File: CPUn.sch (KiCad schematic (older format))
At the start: 11 parts, among them J4 JTAG

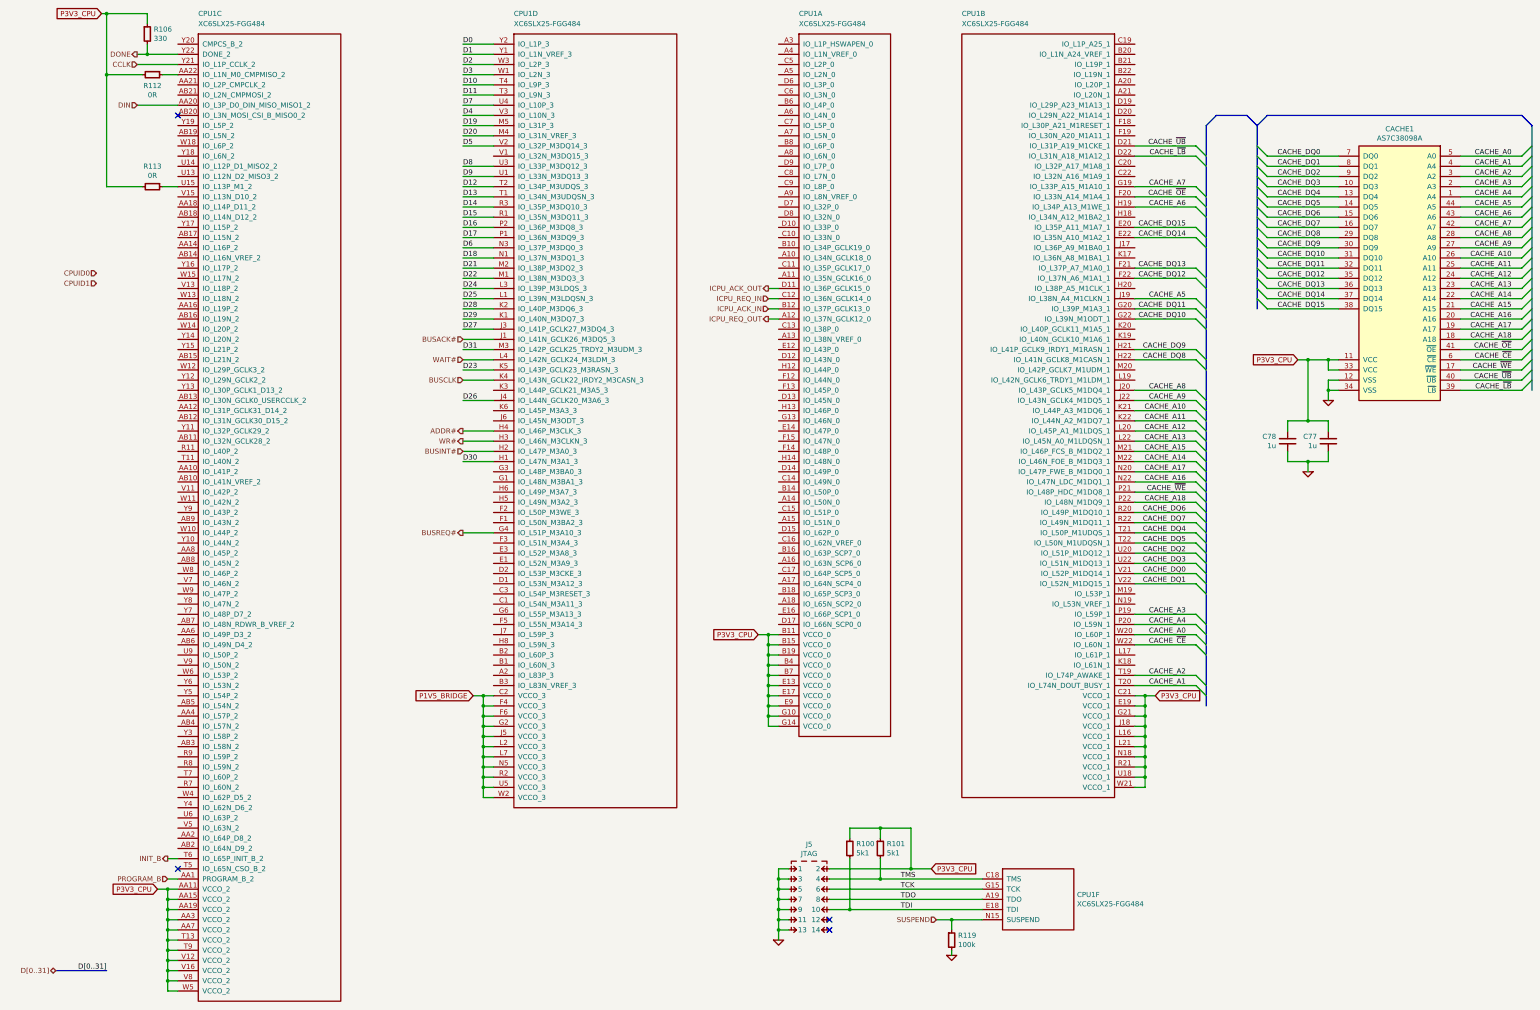
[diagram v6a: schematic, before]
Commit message: Rename active-low signals for consistency
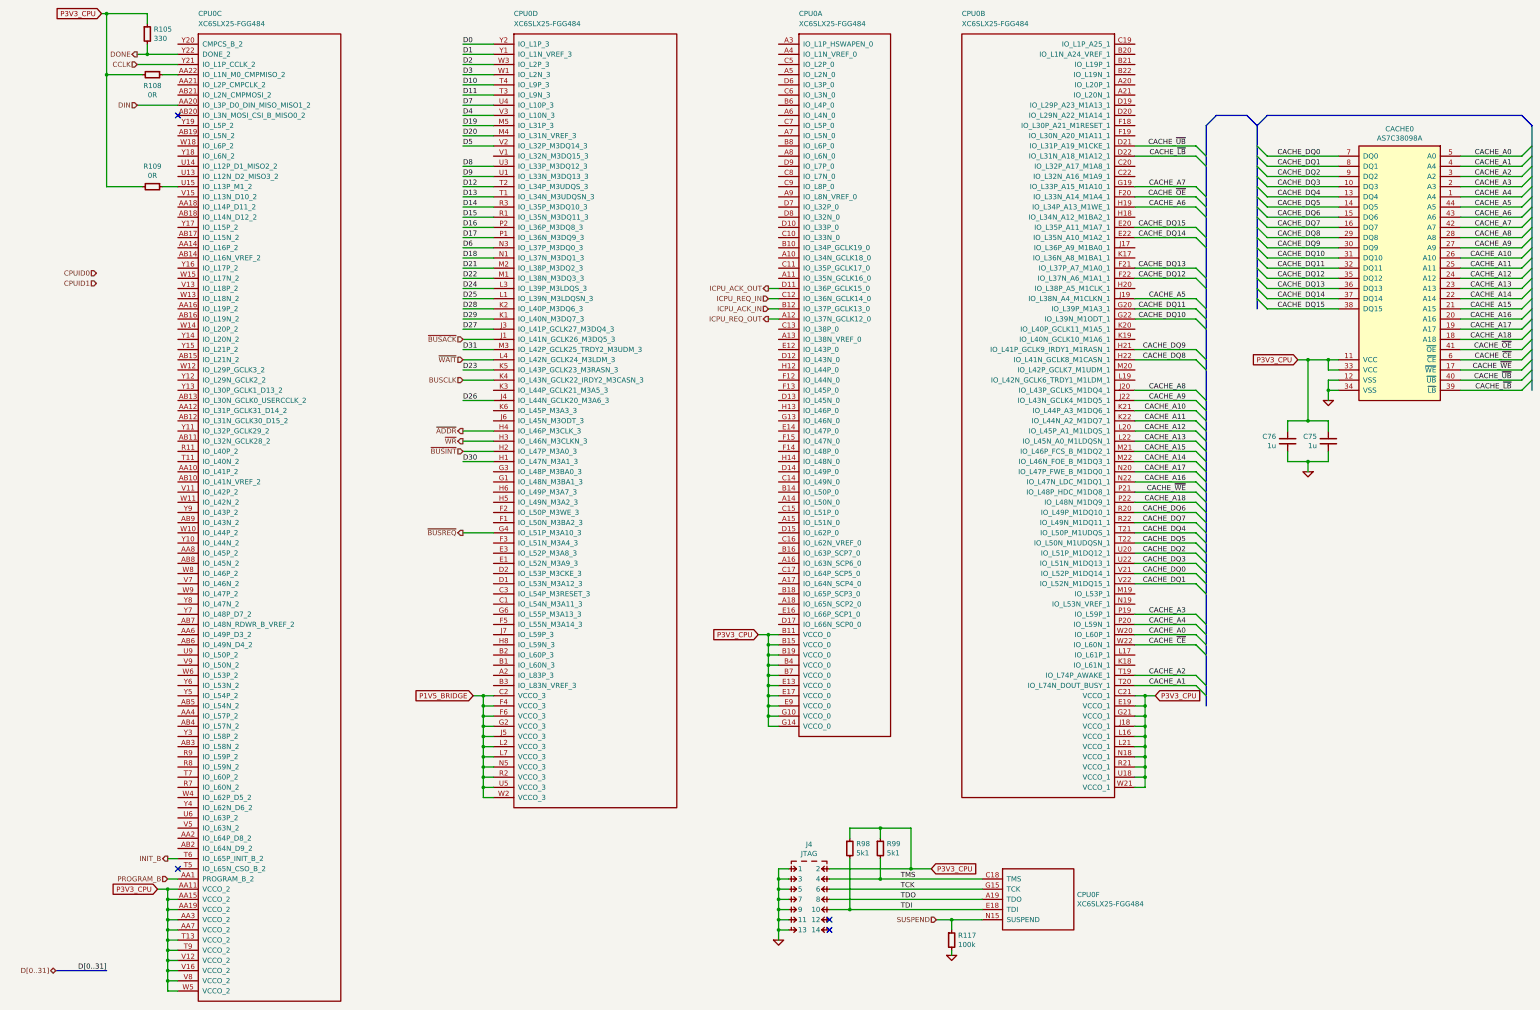
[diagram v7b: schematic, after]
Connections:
- net ADDR# renamed ~ADDR
- net BUSACK# renamed ~BUSACK
- net BUSINT# renamed ~BUSINT
- net BUSREQ# renamed ~BUSREQ
- net WAIT# renamed ~WAIT
- net WR# renamed ~WR
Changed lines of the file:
@@
 $Descr B 17000 11000
 encoding utf-8
-Sheet 9 10
+Sheet 4 10
 Title "CPU"
 Date "2016-08-05"
@@
 AR Path="/5765A5BA/577B458D" Ref="CPU0"  Part="3"
 AR Path="/5765B2E6/577B458D" Ref="CPU1"  Part="3"
-F 0 "CPU1" H 2500 1300 50  0000 L CNN
+F 0 "CPU0" H 2500 1300 50  0000 L CNN
 F 1 "XC6SLX25-FGG484" H 2500 1200 50  0000 L CNN
 F 2 "manuf:XILINX-FGG484" H 2400 1150 50  0001 C CNN
@@
 D[0..31]
 Text HLabel 5100 4100 0    50   Input ~ 0
-WAIT#
+~WAIT
 Text HLabel 5100 4800 0    50   Output ~ 0
-ADDR#
+~ADDR
 Text HLabel 5100 4900 0    50   Output ~ 0
-WR#
+~WR
 Text HLabel 5100 5800 0    50   Output ~ 0
-BUSREQ#
+~BUSREQ
 Text HLabel 5100 3900 0    50   Input ~ 0
-BUSACK#
+~BUSACK
 Text HLabel 5100 5000 0    50   Input ~ 0
-BUSINT#
+~BUSINT
 Text GLabel 2100 9300 0    50   Input ~ 0
 P3V3_CPU
@@
 AR Path="/5765A5BA/5783D342" Ref="CACHE0"  Part="1"
 AR Path="/5765B2E6/5783D342" Ref="CACHE1"  Part="1"
-F 0 "CACHE1" H 14300 2367 50  0000 C CNN
+F 0 "CACHE0" H 14300 2367 50  0000 C CNN
 F 1 "AS7C38098A" H 14300 2276 50  0000 C CNN
 F 2 "IPC7351-Nominal:SOP80P1176X120-44" H 14300 -400 50  0001 C CNN
@@
 AR Path="/5765A5BA/5793B4AE" Ref="#PWR122"  Part="1"
 AR Path="/5765B2E6/5793B4AE" Ref="#PWR184"  Part="1"
-F 0 "#PWR184" H 13600 4500 30  0001 C CNN
+F 0 "#PWR122" H 13600 4500 30  0001 C CNN
 F 1 "GND" H 13600 4430 30  0001 C CNN
 F 2 "" H 13600 4500 60  0000 C CNN
@@
 AR Path="/5765A5BA/5793BAAD" Ref="C75"  Part="1"
 AR Path="/5765B2E6/5793BAAD" Ref="C77"  Part="1"
-F 0 "C77" H 13712 4946 50  0000 L CNN
+F 0 "C75" H 13712 4946 50  0000 L CNN
 F 1 "1u" H 13712 4855 50  0000 L CNN
 F 2 "IPC7351-Nominal:CAPC1005X55" H 13600 4900 50  0001 C CNN
@@
 AR Path="/5765A5BA/5793BB4A" Ref="C76"  Part="1"
 AR Path="/5765B2E6/5793BB4A" Ref="C78"  Part="1"
-F 0 "C78" H 13313 4946 50  0000 L CNN
+F 0 "C76" H 13313 4946 50  0000 L CNN
 F 1 "1u" H 13313 4855 50  0000 L CNN
 F 2 "IPC7351-Nominal:CAPC1005X55" H 13200 4900 50  0001 C CNN
@@
 AR Path="/5765A5BA/5793BC86" Ref="#PWR121"  Part="1"
 AR Path="/5765B2E6/5793BC86" Ref="#PWR183"  Part="1"
-F 0 "#PWR183" H 13400 5200 30  0001 C CNN
+F 0 "#PWR121" H 13400 5200 30  0001 C CNN
 F 1 "GND" H 13400 5130 30  0001 C CNN
 F 2 "" H 13400 5200 60  0000 C CNN
@@
 AR Path="/5765A5BA/57942A58" Ref="CPU0"  Part="4"
 AR Path="/5765B2E6/57942A58" Ref="CPU1"  Part="4"
-F 0 "CPU1" H 5600 1300 50  0000 L CNN
+F 0 "CPU0" H 5600 1300 50  0000 L CNN
 F 1 "XC6SLX25-FGG484" H 5600 1200 50  0000 L CNN
 F 2 "manuf:XILINX-FGG484" H 5500 1150 50  0001 C CNN
@@
 AR Path="/5765A5BA/5795C53B" Ref="CPU0"  Part="1"
 AR Path="/5765B2E6/5795C53B" Ref="CPU1"  Part="1"
-F 0 "CPU1" H 8400 1300 50  0000 L CNN
+F 0 "CPU0" H 8400 1300 50  0000 L CNN
 F 1 "XC6SLX25-FGG484" H 8400 1200 50  0000 L CNN
 F 2 "manuf:XILINX-FGG484" H 8300 1150 50  0001 C CNN
@@
 AR Path="/5765A5BA/5795C751" Ref="CPU0"  Part="2"
 AR Path="/5765B2E6/5795C751" Ref="CPU1"  Part="2"
-F 0 "CPU1" H 13400 1300 50  0000 R CNN
+F 0 "CPU0" H 13400 1300 50  0000 R CNN
 F 1 "XC6SLX25-FGG484" H 13400 1200 50  0000 R CNN
 F 2 "manuf:XILINX-FGG484" H 11800 1150 50  0001 C CNN
@@
 AR Path="/5765A5BA/57A58F79" Ref="R105"  Part="1"
 AR Path="/5765B2E6/57A58F79" Ref="R106"  Part="1"
-F 0 "R106" H 2063 946 50  0000 L CNN
+F 0 "R105" H 2063 946 50  0000 L CNN
 F 1 "330" H 2063 855 50  0000 L CNN
 F 2 "IPC7351-Nominal:RESC1005X40" H 2000 900 50  0001 C CNN
@@
 AR Path="/5765A5BA/57A5D20B" Ref="R108"  Part="1"
 AR Path="/5765B2E6/57A5D20B" Ref="R112"  Part="1"
-F 0 "R112" V 2158 1300 50  0000 C CNN
+F 0 "R108" V 2158 1300 50  0000 C CNN
 F 1 "0R" V 2249 1300 50  0000 C CNN
 F 2 "IPC7351-Nominal:RESC1005X40" H 2050 1300 50  0001 C CNN
@@
 AR Path="/5765A5BA/57A5D251" Ref="R109"  Part="1"
 AR Path="/5765B2E6/57A5D251" Ref="R113"  Part="1"
-F 0 "R113" V 1850 2400 50  0000 C CNN
+F 0 "R109" V 1850 2400 50  0000 C CNN
 F 1 "0R" V 1941 2400 50  0000 C CNN
 F 2 "IPC7351-Nominal:RESC1005X40" H 2050 2400 50  0001 C CNN
@@
 AR Path="/5765A5BA/57A7F2F7" Ref="J4"  Part="1"
 AR Path="/5765B2E6/57A7F2F7" Ref="J5"  Part="1"
-F 0 "J5" H 8500 9340 50  0000 C CNN
+F 0 "J4" H 8500 9340 50  0000 C CNN
 F 1 "JTAG" H 8500 9249 50  0000 C CNN
 F 2 "conn-fci:98424-G52-14ALF" H 8475 9100 50  0001 C CNN
@@
 AR Path="/5765B2E6/57A7F302" Ref="#PWR181"  Part="1"
 AR Path="/5765A5BA/57A7F302" Ref="#PWR119"  Part="1"
-F 0 "#PWR181" H 8200 9800 30  0001 C CNN
+F 0 "#PWR119" H 8200 9800 30  0001 C CNN
 F 1 "GND" H 8200 9730 30  0001 C CNN
 F 2 "" H 8200 9800 60  0000 C CNN
@@
 AR Path="/5765A5BA/57A7F317" Ref="R98"  Part="1"
 AR Path="/5765B2E6/57A7F317" Ref="R100"  Part="1"
-F 0 "R100" H 8963 8946 50  0000 L CNN
+F 0 "R98" H 8963 8946 50  0000 L CNN
 F 1 "5k1" H 8963 8855 50  0000 L CNN
 F 2 "IPC7351-Nominal:RESC1005X40" H 8900 8900 50  0001 C CNN
@@
 AR Path="/5765A5BA/57A7F321" Ref="R99"  Part="1"
 AR Path="/5765B2E6/57A7F321" Ref="R101"  Part="1"
-F 0 "R101" H 9263 8946 50  0000 L CNN
+F 0 "R99" H 9263 8946 50  0000 L CNN
 F 1 "5k1" H 9263 8855 50  0000 L CNN
 F 2 "IPC7351-Nominal:RESC1005X40" H 9200 8900 50  0001 C CNN
@@
 AR Path="/5765A5BA/57A7F34A" Ref="CPU0"  Part="6"
 AR Path="/5765B2E6/57A7F34A" Ref="CPU1"  Part="6"
-F 0 "CPU1" H 11131 9046 50  0000 L CNN
+F 0 "CPU0" H 11131 9046 50  0000 L CNN
 F 1 "XC6SLX25-FGG484" H 11131 8955 50  0000 L CNN
 F 2 "manuf:XILINX-FGG484" H 10300 9350 50  0001 C CNN
@@
 AR Path="/5765A5BA/57A6CB4C" Ref="R117"  Part="1"
 AR Path="/5765B2E6/57A6CB4C" Ref="R119"  Part="1"
-F 0 "R119" H 9963 9846 50  0000 L CNN
+F 0 "R117" H 9963 9846 50  0000 L CNN
 F 1 "100k" H 9963 9755 50  0000 L CNN
 F 2 "IPC7351-Nominal:RESC1005X40" H 9900 9800 50  0001 C CNN
@@
 AR Path="/5765A5BA/57A6CCC5" Ref="#PWR120"  Part="1"
 AR Path="/5765B2E6/57A6CCC5" Ref="#PWR182"  Part="1"
-F 0 "#PWR182" H 9900 9950 30  0001 C CNN
+F 0 "#PWR120" H 9900 9950 30  0001 C CNN
 F 1 "GND" H 9900 9880 30  0001 C CNN
 F 2 "" H 9900 9950 60  0000 C CNN

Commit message: Route unused PCI JTAG lines
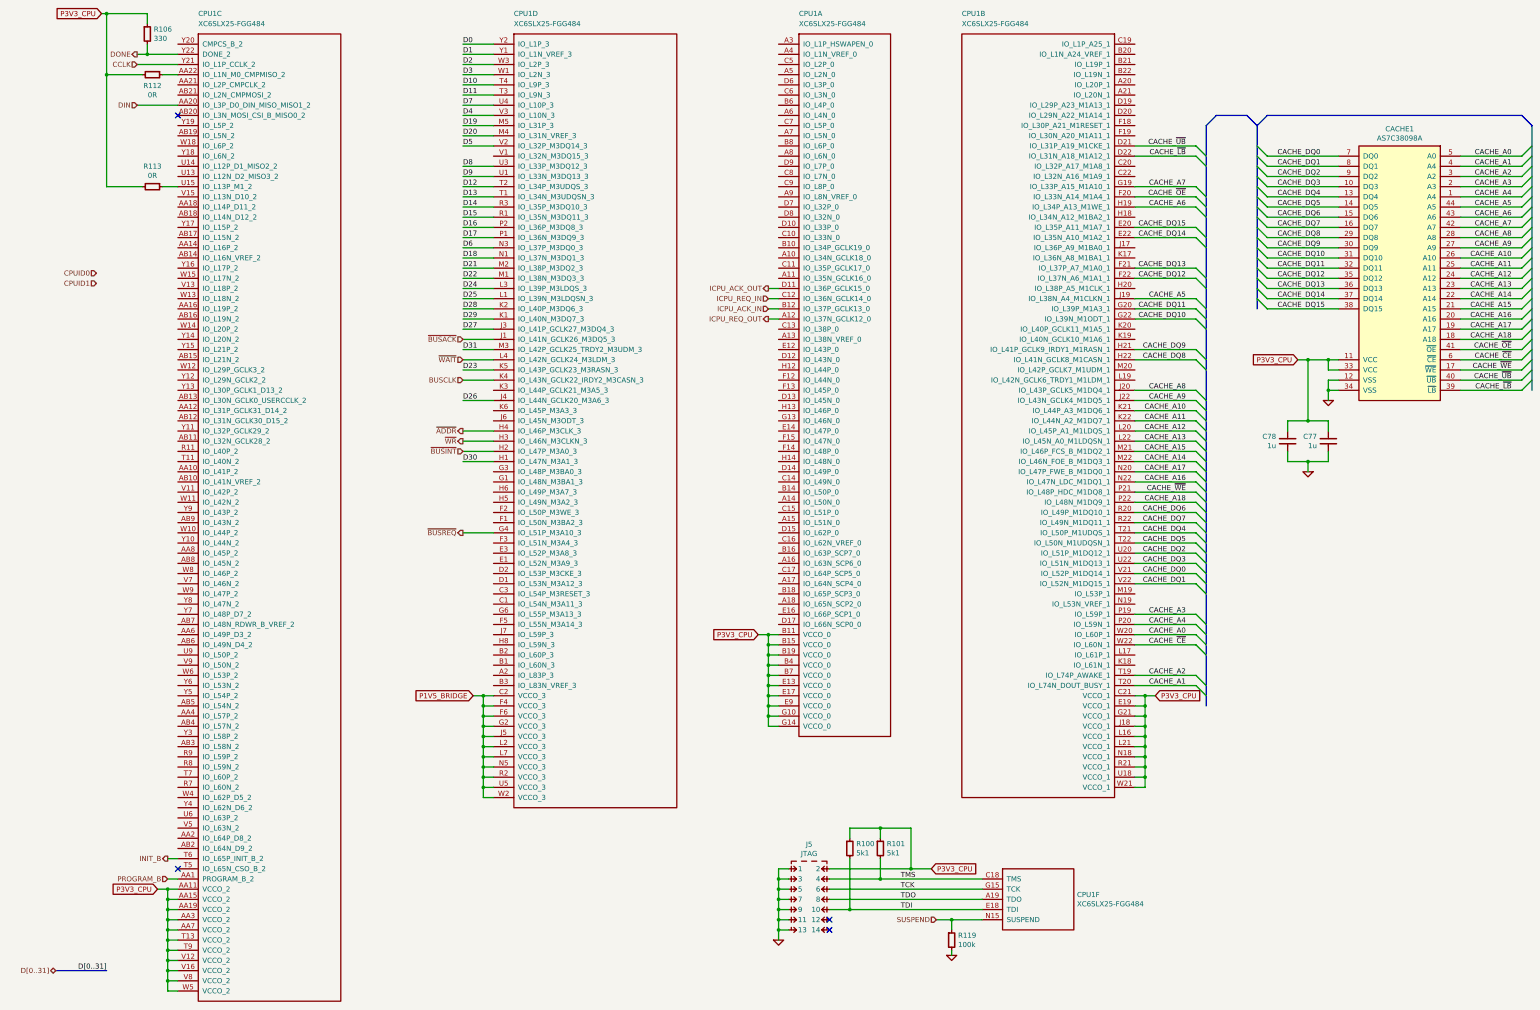
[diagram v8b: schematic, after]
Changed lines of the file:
@@
 AR Path="/5765A5BA/577B458D" Ref="CPU0"  Part="3"
 AR Path="/5765B2E6/577B458D" Ref="CPU1"  Part="3"
-F 0 "CPU0" H 2500 1300 50  0000 L CNN
+F 0 "CPU1" H 2500 1300 50  0000 L CNN
 F 1 "XC6SLX25-FGG484" H 2500 1200 50  0000 L CNN
 F 2 "manuf:XILINX-FGG484" H 2400 1150 50  0001 C CNN
@@
 AR Path="/5765A5BA/5783D342" Ref="CACHE0"  Part="1"
 AR Path="/5765B2E6/5783D342" Ref="CACHE1"  Part="1"
-F 0 "CACHE0" H 14300 2367 50  0000 C CNN
+F 0 "CACHE1" H 14300 2367 50  0000 C CNN
 F 1 "AS7C38098A" H 14300 2276 50  0000 C CNN
 F 2 "IPC7351-Nominal:SOP80P1176X120-44" H 14300 -400 50  0001 C CNN
@@
 P3V3_CPU
 $Comp
-L GND #PWR122
+L GND #PWR123
 U 1 1 5793B4AE
 P 13600 4500
-AR Path="/5765A5BA/5793B4AE" Ref="#PWR122"  Part="1"
-AR Path="/5765B2E6/5793B4AE" Ref="#PWR184"  Part="1"
-F 0 "#PWR122" H 13600 4500 30  0001 C CNN
+AR Path="/5765A5BA/5793B4AE" Ref="#PWR123"  Part="1"
+AR Path="/5765B2E6/5793B4AE" Ref="#PWR181"  Part="1"
+F 0 "#PWR181" H 13600 4500 30  0001 C CNN
 F 1 "GND" H 13600 4430 30  0001 C CNN
 F 2 "" H 13600 4500 60  0000 C CNN
@@
 AR Path="/5765A5BA/5793BAAD" Ref="C75"  Part="1"
 AR Path="/5765B2E6/5793BAAD" Ref="C77"  Part="1"
-F 0 "C75" H 13712 4946 50  0000 L CNN
+F 0 "C77" H 13712 4946 50  0000 L CNN
 F 1 "1u" H 13712 4855 50  0000 L CNN
 F 2 "IPC7351-Nominal:CAPC1005X55" H 13600 4900 50  0001 C CNN
@@
 AR Path="/5765A5BA/5793BB4A" Ref="C76"  Part="1"
 AR Path="/5765B2E6/5793BB4A" Ref="C78"  Part="1"
-F 0 "C76" H 13313 4946 50  0000 L CNN
+F 0 "C78" H 13313 4946 50  0000 L CNN
 F 1 "1u" H 13313 4855 50  0000 L CNN
 F 2 "IPC7351-Nominal:CAPC1005X55" H 13200 4900 50  0001 C CNN
@@
 $EndComp
 $Comp
-L GND #PWR121
+L GND #PWR122
 U 1 1 5793BC86
 P 13400 5200
-AR Path="/5765A5BA/5793BC86" Ref="#PWR121"  Part="1"
-AR Path="/5765B2E6/5793BC86" Ref="#PWR183"  Part="1"
-F 0 "#PWR121" H 13400 5200 30  0001 C CNN
+AR Path="/5765A5BA/5793BC86" Ref="#PWR122"  Part="1"
+AR Path="/5765B2E6/5793BC86" Ref="#PWR180"  Part="1"
+F 0 "#PWR180" H 13400 5200 30  0001 C CNN
 F 1 "GND" H 13400 5130 30  0001 C CNN
 F 2 "" H 13400 5200 60  0000 C CNN
@@
 AR Path="/5765A5BA/57942A58" Ref="CPU0"  Part="4"
 AR Path="/5765B2E6/57942A58" Ref="CPU1"  Part="4"
-F 0 "CPU0" H 5600 1300 50  0000 L CNN
+F 0 "CPU1" H 5600 1300 50  0000 L CNN
 F 1 "XC6SLX25-FGG484" H 5600 1200 50  0000 L CNN
 F 2 "manuf:XILINX-FGG484" H 5500 1150 50  0001 C CNN
@@
 AR Path="/5765A5BA/5795C53B" Ref="CPU0"  Part="1"
 AR Path="/5765B2E6/5795C53B" Ref="CPU1"  Part="1"
-F 0 "CPU0" H 8400 1300 50  0000 L CNN
+F 0 "CPU1" H 8400 1300 50  0000 L CNN
 F 1 "XC6SLX25-FGG484" H 8400 1200 50  0000 L CNN
 F 2 "manuf:XILINX-FGG484" H 8300 1150 50  0001 C CNN
@@
 AR Path="/5765A5BA/5795C751" Ref="CPU0"  Part="2"
 AR Path="/5765B2E6/5795C751" Ref="CPU1"  Part="2"
-F 0 "CPU0" H 13400 1300 50  0000 R CNN
+F 0 "CPU1" H 13400 1300 50  0000 R CNN
 F 1 "XC6SLX25-FGG484" H 13400 1200 50  0000 R CNN
 F 2 "manuf:XILINX-FGG484" H 11800 1150 50  0001 C CNN
@@
 AR Path="/5765A5BA/57A58F79" Ref="R105"  Part="1"
 AR Path="/5765B2E6/57A58F79" Ref="R106"  Part="1"
-F 0 "R105" H 2063 946 50  0000 L CNN
+F 0 "R106" H 2063 946 50  0000 L CNN
 F 1 "330" H 2063 855 50  0000 L CNN
 F 2 "IPC7351-Nominal:RESC1005X40" H 2000 900 50  0001 C CNN
@@
 AR Path="/5765A5BA/57A5D20B" Ref="R108"  Part="1"
 AR Path="/5765B2E6/57A5D20B" Ref="R112"  Part="1"
-F 0 "R108" V 2158 1300 50  0000 C CNN
+F 0 "R112" V 2158 1300 50  0000 C CNN
 F 1 "0R" V 2249 1300 50  0000 C CNN
 F 2 "IPC7351-Nominal:RESC1005X40" H 2050 1300 50  0001 C CNN
@@
 AR Path="/5765A5BA/57A5D251" Ref="R109"  Part="1"
 AR Path="/5765B2E6/57A5D251" Ref="R113"  Part="1"
-F 0 "R109" V 1850 2400 50  0000 C CNN
+F 0 "R113" V 1850 2400 50  0000 C CNN
 F 1 "0R" V 1941 2400 50  0000 C CNN
 F 2 "IPC7351-Nominal:RESC1005X40" H 2050 2400 50  0001 C CNN
@@
 AR Path="/5765A5BA/57A7F2F7" Ref="J4"  Part="1"
 AR Path="/5765B2E6/57A7F2F7" Ref="J5"  Part="1"
-F 0 "J4" H 8500 9340 50  0000 C CNN
+F 0 "J5" H 8500 9340 50  0000 C CNN
 F 1 "JTAG" H 8500 9249 50  0000 C CNN
 F 2 "conn-fci:98424-G52-14ALF" H 8475 9100 50  0001 C CNN
@@
 P 8200 9800
 AR Path="/5763AB3B/57A7F302" Ref="#PWR?"  Part="1"
-AR Path="/5765B2E6/57A7F302" Ref="#PWR181"  Part="1"
-AR Path="/5765A5BA/57A7F302" Ref="#PWR119"  Part="1"
-F 0 "#PWR119" H 8200 9800 30  0001 C CNN
+AR Path="/5765B2E6/57A7F302" Ref="#PWR178"  Part="1"
+AR Path="/5765A5BA/57A7F302" Ref="#PWR120"  Part="1"
+F 0 "#PWR178" H 8200 9800 30  0001 C CNN
 F 1 "GND" H 8200 9730 30  0001 C CNN
 F 2 "" H 8200 9800 60  0000 C CNN
@@
 AR Path="/5765A5BA/57A7F317" Ref="R98"  Part="1"
 AR Path="/5765B2E6/57A7F317" Ref="R100"  Part="1"
-F 0 "R98" H 8963 8946 50  0000 L CNN
+F 0 "R100" H 8963 8946 50  0000 L CNN
 F 1 "5k1" H 8963 8855 50  0000 L CNN
 F 2 "IPC7351-Nominal:RESC1005X40" H 8900 8900 50  0001 C CNN
@@
 AR Path="/5765A5BA/57A7F321" Ref="R99"  Part="1"
 AR Path="/5765B2E6/57A7F321" Ref="R101"  Part="1"
-F 0 "R99" H 9263 8946 50  0000 L CNN
+F 0 "R101" H 9263 8946 50  0000 L CNN
 F 1 "5k1" H 9263 8855 50  0000 L CNN
 F 2 "IPC7351-Nominal:RESC1005X40" H 9200 8900 50  0001 C CNN
@@
 AR Path="/5765A5BA/57A7F34A" Ref="CPU0"  Part="6"
 AR Path="/5765B2E6/57A7F34A" Ref="CPU1"  Part="6"
-F 0 "CPU0" H 11131 9046 50  0000 L CNN
+F 0 "CPU1" H 11131 9046 50  0000 L CNN
 F 1 "XC6SLX25-FGG484" H 11131 8955 50  0000 L CNN
 F 2 "manuf:XILINX-FGG484" H 10300 9350 50  0001 C CNN
@@
 AR Path="/5765A5BA/57A6CB4C" Ref="R117"  Part="1"
 AR Path="/5765B2E6/57A6CB4C" Ref="R119"  Part="1"
-F 0 "R117" H 9963 9846 50  0000 L CNN
+F 0 "R119" H 9963 9846 50  0000 L CNN
 F 1 "100k" H 9963 9755 50  0000 L CNN
 F 2 "IPC7351-Nominal:RESC1005X40" H 9900 9800 50  0001 C CNN
@@
 	9900 9600 9900 9700
 $Comp
-L GND #PWR120
+L GND #PWR121
 U 1 1 57A6CCC5
 P 9900 9950
-AR Path="/5765A5BA/57A6CCC5" Ref="#PWR120"  Part="1"
-AR Path="/5765B2E6/57A6CCC5" Ref="#PWR182"  Part="1"
-F 0 "#PWR120" H 9900 9950 30  0001 C CNN
+AR Path="/5765A5BA/57A6CCC5" Ref="#PWR121"  Part="1"
+AR Path="/5765B2E6/57A6CCC5" Ref="#PWR179"  Part="1"
+F 0 "#PWR179" H 9900 9950 30  0001 C CNN
 F 1 "GND" H 9900 9880 30  0001 C CNN
 F 2 "" H 9900 9950 60  0000 C CNN
